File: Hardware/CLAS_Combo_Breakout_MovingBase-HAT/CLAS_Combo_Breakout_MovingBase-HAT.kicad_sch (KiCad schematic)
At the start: 61 parts, among them J1 USB_C_Receptacle_USB2.0, J2 ZED, J3 NEO, U1 USBLC6-2P6

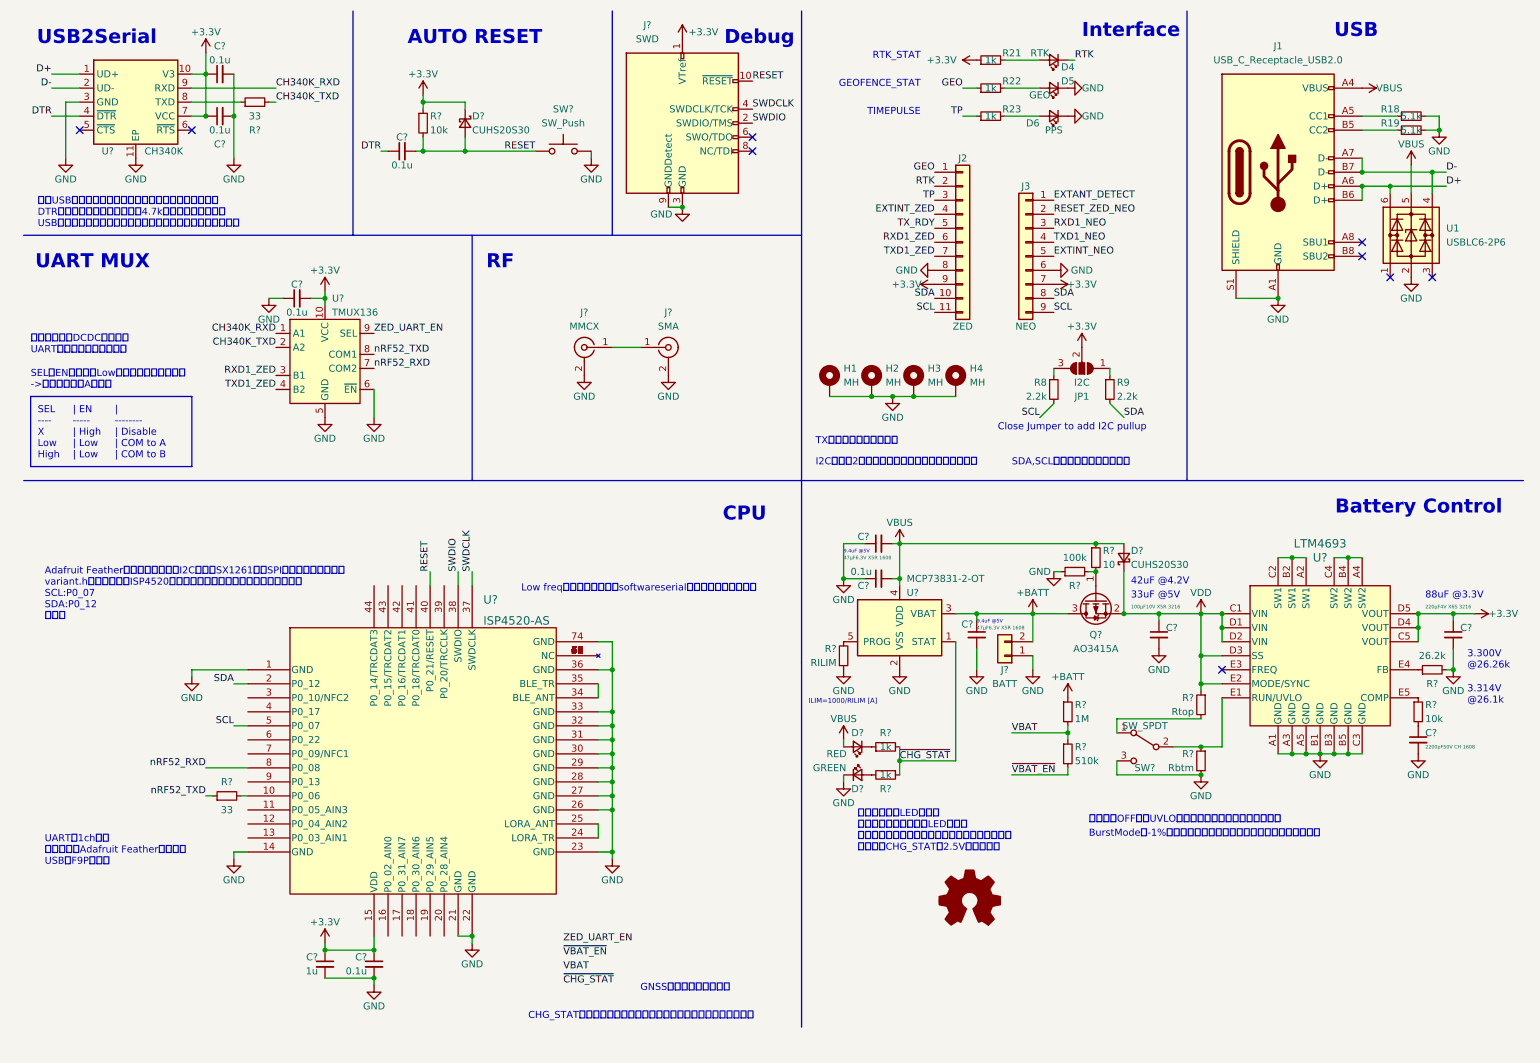
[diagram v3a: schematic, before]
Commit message: アノテーション完了、一部のピンは仮結線
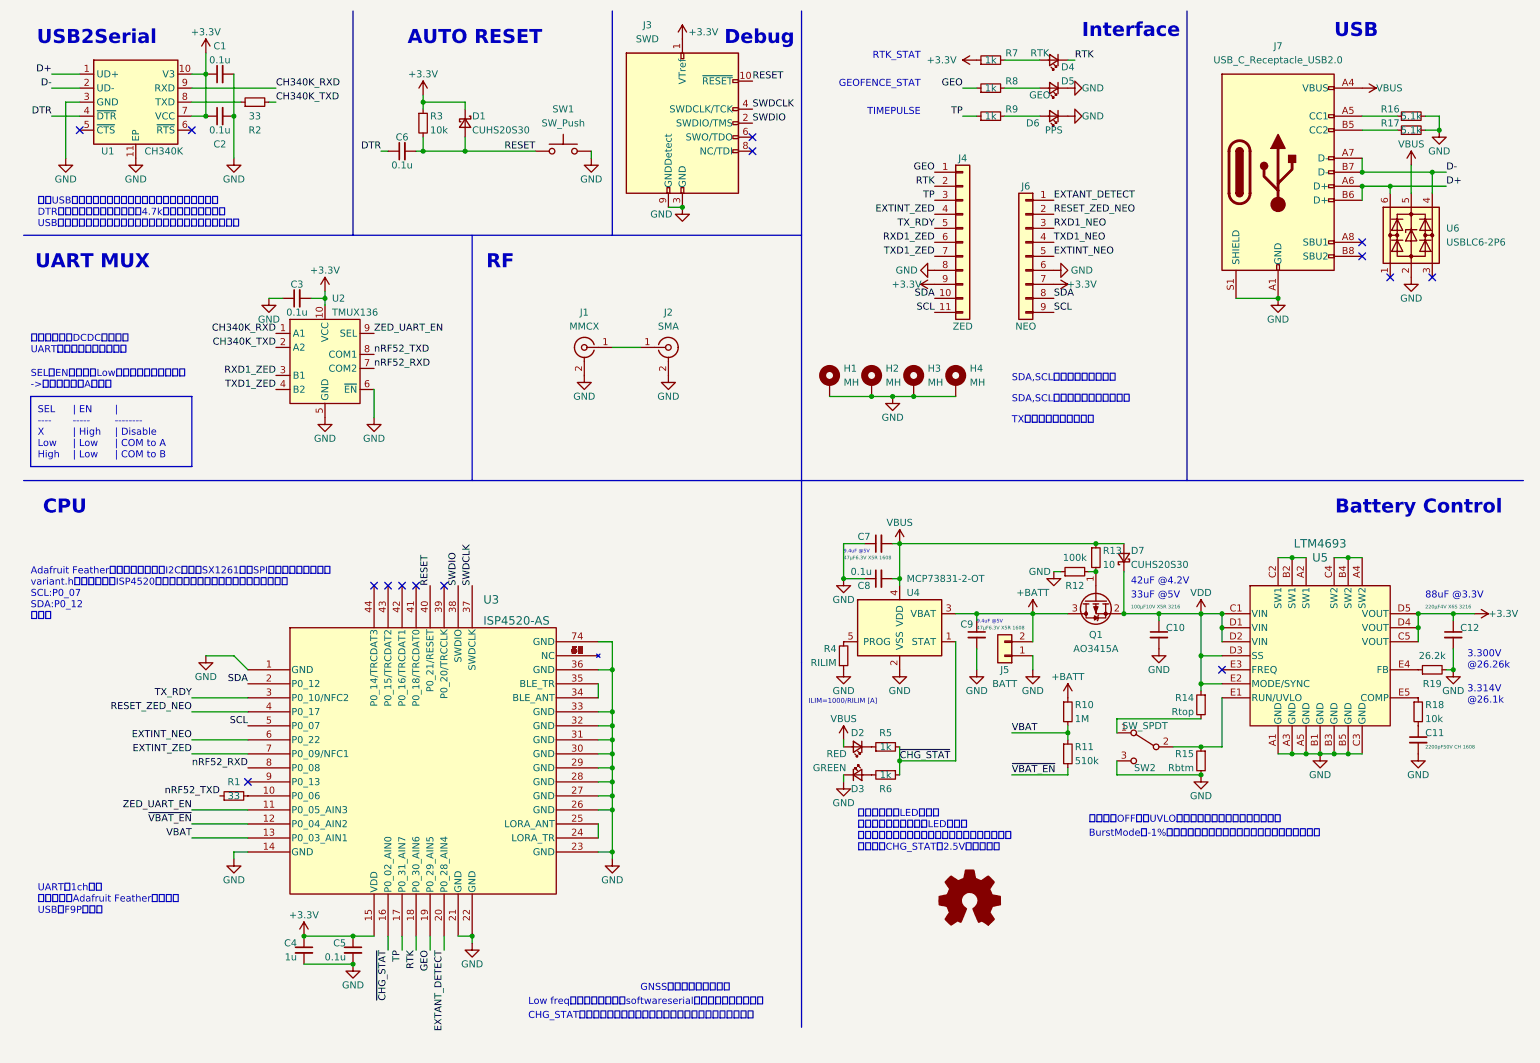
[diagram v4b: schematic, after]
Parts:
- removed JP1: I2C, Jumper_extlib:SolderJumper-3_Open_RoundedPad, symbol Jumper:SolderJumper_3_Open
- removed R8, R9: 2.2k, Resistor_SMD:R_0603_1608Metric, symbol Device:R_Small
- gave numbers to parts that had none: 42
- renumbered J2 to J4, J3 to J6, J1 to J7, R18 to R16, R19 to R17, R21 to R7, R22 to R8, R23 to R9, U1 to U6
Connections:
- net EXTANT_DETECT: now also U3.20 (P0_28_AIN4)
- net EXTINT_NEO: now also U3.6 (P0_22)
- net EXTINT_ZED: now also U3.7 (P0_09/NFC1)
- net GEO: now also U3.19 (P0_29_AIN5)
- net RESET_ZED_NEO: now also U3.4 (P0_17)
- net RTK: now also U3.18 (P0_30_AIN6)
- net TP: now also U3.17 (P0_31_AIN7)
- net TX_RDY: now also U3.3 (P0_10/NFC2)
- net VBAT: now also U3.13 (P0_03_AIN1)
- net ZED_UART_EN: now also U3.11 (P0_05_AIN3)
- net ~{CHG_STAT}: now also U3.16 (P0_02_AIN0)
- net ~{VBAT_EN}: now also U3.12 (P0_04_AIN2)
- no-connect marks 9 -> 15
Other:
- note added: "SDA,SCLは片方だけ配線する"
- note removed: "Close Jumper to add I2C pullup"
- note removed: "I2Cピンは2セットあるから配線しやすい方を使う"
- moved on the sheet: C4, C5, R1

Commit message: フットプリントの割り当て完了
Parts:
- C1, C2, C3, C4, C5, C6, C7, C8, C9: footprint (none) -> Capacitor_SMD:C_0603_1608Metric
- J1: footprint (none) -> Connector_Coaxial_extlib:MMCX_Samtec_MMCX-P-P-H-ST-SM1_Male
- J2: footprint (none) -> Connector_Coaxial_extlib:SMA_Molex_0732512440_embed
- J3: footprint (none) -> Connector_PinHeader_1.27mm:PinHeader_2x05_P1.27mm_Horizontal
- J5: footprint (none) -> Connector_JST:JST_PH_S2B-PH-K_1x02_P2.00mm_Horizontal
- Q1: footprint (none) -> Package_TO_SOT_SMD:SOT-23
- R1, R10, R11, R13, R14, R15, R18, R2, R3, R4: footprint (none) -> Resistor_SMD:R_0603_1608Metric
- SW1: footprint (none) -> Button_Switch_SMD:SW_Push_1P1T_NO_Vertical_Wuerth_434133025816
- SW2: footprint (none) -> Button_Switch_THT_extlib:NKK_SS-12SDP2
- U1: footprint (none) -> Package_SO:SSOP-10_3.9x4.9mm_P1.00mm
- U2: footprint (none) -> Package_DFN_QFN:Texas_R-PUQFN-N10
- U3: footprint (none) -> RF_Module_extlib:ISP4520-AS
- U5: footprint (none) -> Converter_DCDC_extlib:Converter_DCDC_AnalogDevices_LTM4693

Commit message: 配線４割
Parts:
- J3: footprint Connector_PinHeader_1.27mm:PinHeader_2x05_P1.27mm_Horizontal -> Connector_PinHeader_1.27mm:PinHeader_2x05_P1.27mm_Vertical
- J5: footprint Connector_JST:JST_PH_S2B-PH-K_1x02_P2.00mm_Horizontal -> Connector_JST:JST_PH_S2B-PH-SM4-TB_1x02-1MP_P2.00mm_Horizontal
- SW2: footprint Button_Switch_THT_extlib:NKK_SS-12SDP2 -> Button_Switch_SMD_extlib:SW_SPDT_SSSS213202
- U3: footprint RF_Module_extlib:ISP4520-AS -> RF_Module_extlib:ISP4520-AS_with_Keep-Out
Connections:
- net D+: now also U6.1 (I/O1)
- net D-: now also U6.3 (I/O2)
- net EXTANT_DETECT: now also U3.4 (P0_17); no longer U3.20 (P0_28_AIN4)
- net EXTINT_ZED: now also U3.18 (P0_30_AIN6); no longer U3.7 (P0_09/NFC1)
- net GEO: now also U3.13 (P0_03_AIN1); no longer U3.19 (P0_29_AIN5)
- net RESET_ZED_NEO: now also U3.3 (P0_10/NFC2); no longer U3.4 (P0_17)
- net RTK: now also U3.16 (P0_02_AIN0); no longer U3.18 (P0_30_AIN6)
- net SCL: no longer J6.9 (Pin_9)
- net SDA: no longer J6.8 (Pin_8)
- net TX_RDY: now also U3.20 (P0_28_AIN4); no longer U3.3 (P0_10/NFC2)
- net VBAT: now also U3.12 (P0_04_AIN2); no longer U3.13 (P0_03_AIN1)
- net ZED_UART_EN: now also U3.7 (P0_09/NFC1); no longer U3.11 (P0_05_AIN3)
- net ~{CHG_STAT}: now also U3.19 (P0_29_AIN5); no longer U3.16 (P0_02_AIN0)
- net ~{VBAT_EN}: now also U3.11 (P0_05_AIN3); no longer U3.12 (P0_04_AIN2)

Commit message: ちょっと配線した
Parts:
- removed C3: 0.1u, Capacitor_SMD:C_0603_1608Metric, symbol Device:C_Small
- removed H4: MH, MountingHole:MountingHole_2.2mm_M2_Pad_Via, symbol Mechanical:MountingHole_Pad
- removed J6: NEO, Connector_PinHeader_2.54mm:PinHeader_1x09_P2.54mm_Vertical, symbol Connector_Generic:Conn_01x09
- added J6: NEO, Connector_PinHeader_2.54mm:PinHeader_1x07_P2.54mm_Vertical, symbol Connector_Generic:Conn_01x07
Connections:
- net +3.3V: now also J6.7 (Pin_7)
- net EXTANT_DETECT: now also J6.1 (Pin_1)
- net EXTINT_NEO: now also J6.5 (Pin_5)
- net GEO: now also U3.11 (P0_05_AIN3); no longer U3.13 (P0_03_AIN1)
- net GND: now also J6.6 (Pin_6)
- net RESET_ZED_NEO: now also J6.2 (Pin_2)
- net RXD1_NEO: now also J6.3 (Pin_3)
- net TXD1_NEO: now also J6.4 (Pin_4)
- net VBAT: now also U3.13 (P0_03_AIN1); no longer U3.12 (P0_04_AIN2)
- net ~{VBAT_EN}: now also U3.12 (P0_04_AIN2); no longer U3.11 (P0_05_AIN3)
- no-connect marks 15 -> 13
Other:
- note added: "パスコンは実装面積の都合でC1を共有"

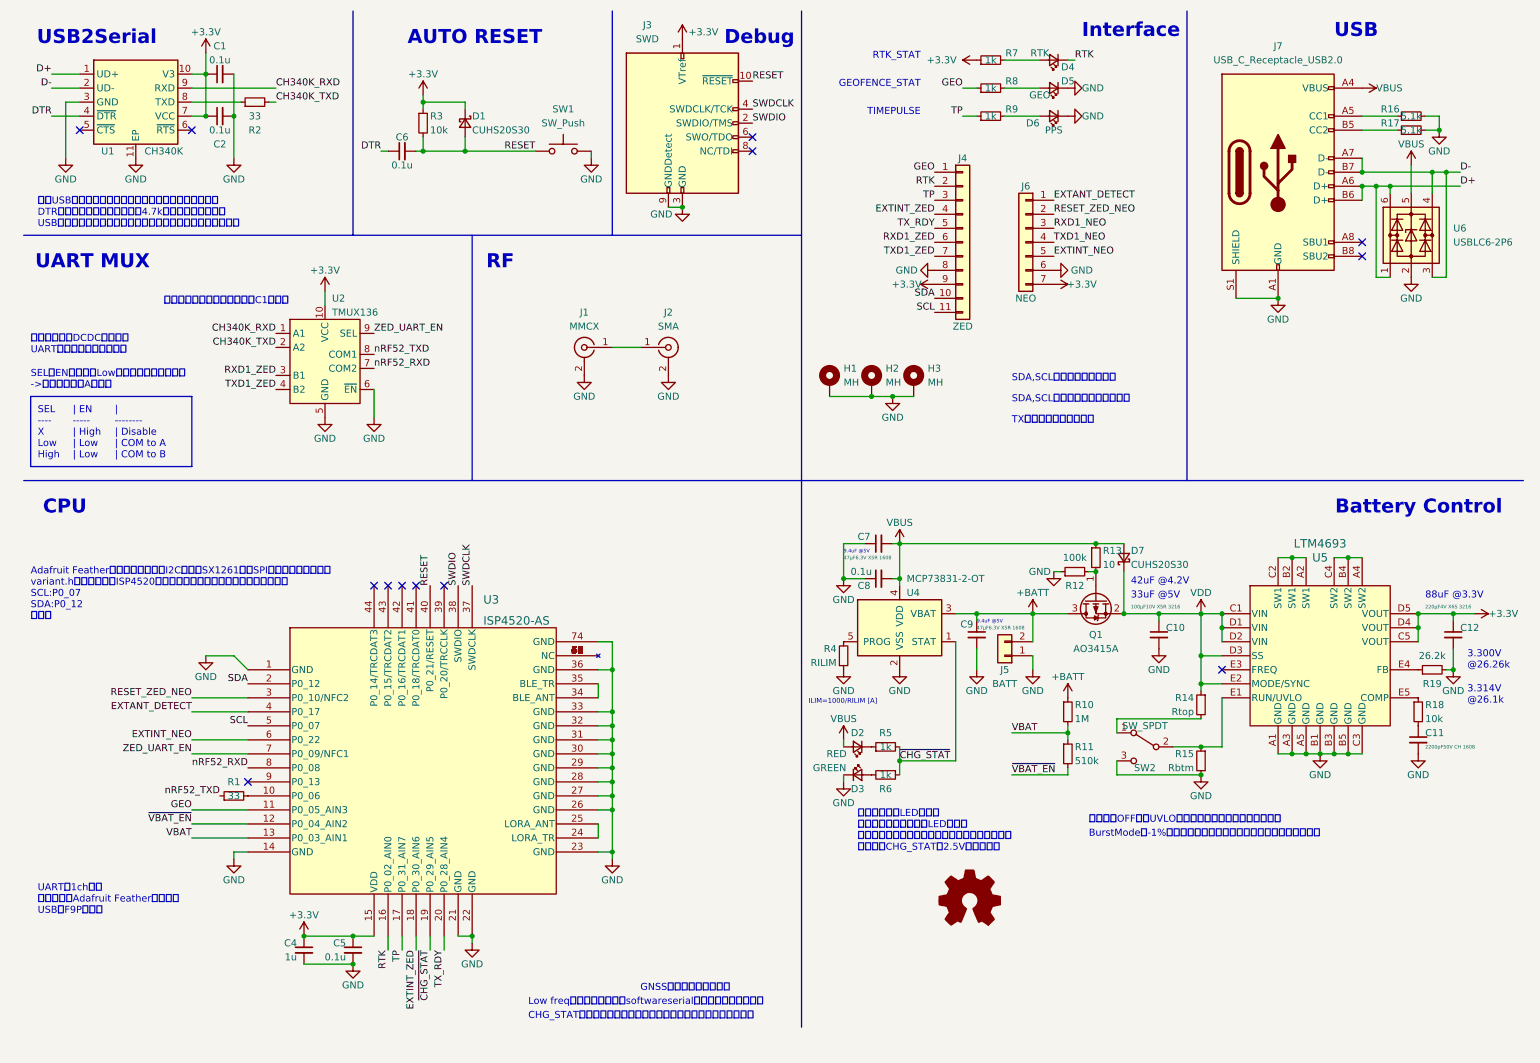
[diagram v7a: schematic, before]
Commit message: MUXをSP3Tのものに変更しRS485経由での補正データの送受信に対応する回路図を書いた
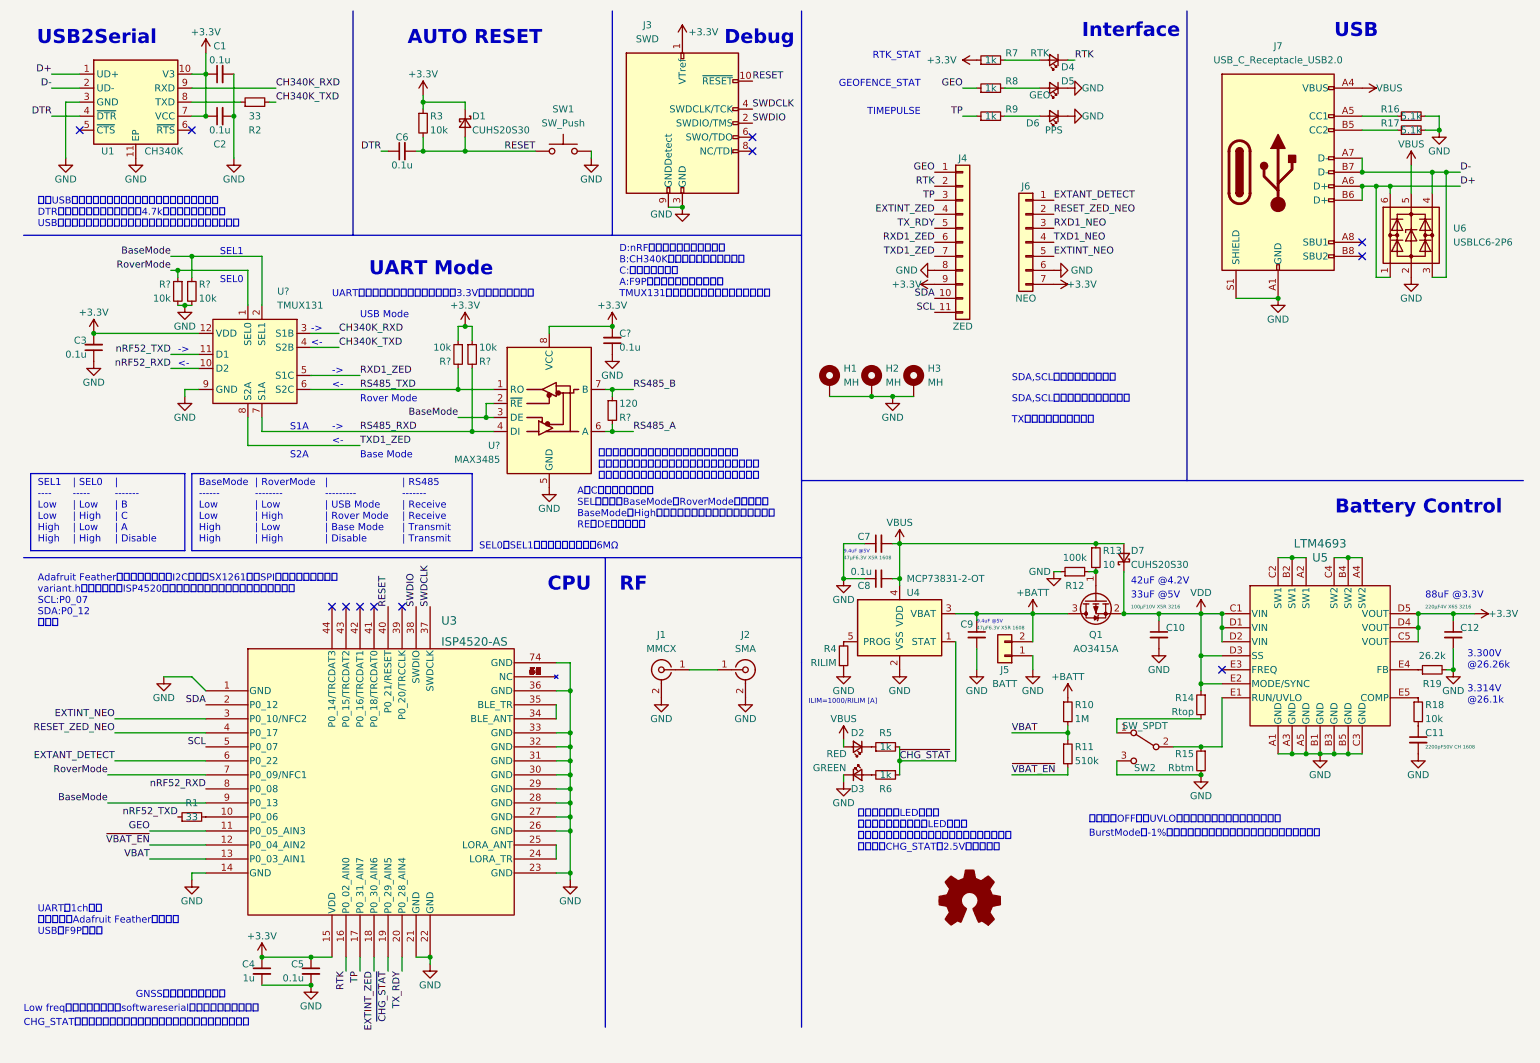
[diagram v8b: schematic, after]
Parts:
- removed U2: TMUX136, Package_DFN_QFN:Texas_R-PUQFN-N10, symbol Analog_Switch_extlib:TMUX136
- added C3, C?: 0.1u, Capacitor_SMD:C_0603_1608Metric, symbol Device:C_Small
- added R? (x4): 10k, Resistor_SMD:R_0603_1608Metric, symbol Device:R_Small
- added R?: 120, Resistor_SMD:R_0603_1608Metric, symbol Device:R_Small
- added U?: TMUX131, symbol Analog_Switch_extlib:TMUX131
- added U?: MAX3485, symbol Interface_UART:MAX3485
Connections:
- net +3.3V: now also C3.2, C?.2, R?.1, R?.1, U?.12 (VDD), U?.8 (VCC)
- net CH340K_RXD: now also U?.3 (S1B)
- net CH340K_TXD: now also U?.4 (S2B)
- net EXTANT_DETECT: now also U3.6 (P0_22); no longer U3.4 (P0_17)
- net EXTINT_NEO: now also U3.3 (P0_10/NFC2); no longer U3.6 (P0_22)
- net GND: now also C3.1, C?.1, R?.2, R?.2, U?.5 (GND), U?.9 (GND)
- net RESET_ZED_NEO: now also U3.4 (P0_17); no longer U3.3 (P0_10/NFC2)
- net RXD1_ZED: now also U?.5 (S1C)
- net TXD1_ZED: now also U?.8 (S2A)
- net nRF52_RXD: now also U?.10 (D2)
- net nRF52_TXD: now also U?.11 (D1)
- net BaseMode: now reaches U3.9 (P0_13)
- net BaseMode: now also R?.1, U?.2 (SEL1), U?.2 (~{RE}), U?.3 (DE)
- net ZED_UART_EN renamed RoverMode
- net RoverMode: now also R?.1, U?.1 (SEL0)
- new net RS485_A: R?.2, U?.6 (A)
- new net RS485_B: R?.1, U?.7 (B)
- new net RS485_RXD: R?.2, U?.4 (DI), U?.7 (S1A)
- new net RS485_TXD: R?.2, U?.1 (RO), U?.6 (S2C)
- no-connect marks 13 -> 12
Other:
- note added: "->"
- note added: "<-"
- note added: "AとCを逆にする場合は SELに繋がるBaseModeとRoverModeを逆にする BaseModeがHighのときに送信するのは変わらないので REとDEはそのまま"
- note added: "Base Mode"
- note added: "BaseMode ------ Low Low High High"
- note added: "D:nRF側送信端だけダンピング B:CH340K側送信端だけダンピング C:ダンピングなし A:F9P送信端にダンピングあり TMUX131側送信端のダンピングは全て省略"
- note added: "Rover Mode"
- note added: "S1A"
- note added: "S2A"
- note added: "SEL0"
- note added: "SEL0とSEL1の内部プルダウンは6MΩ"
- note added: "SEL1"
- note added: "SEL1 ---- Low Low High High"
- note added: "UART Mode"
- note added: "UARTは正論理だが信号が無いときは3.3Vなのでプルアップ"
- note added: "USB Mode"
- note added: "| ------- | B | C | A | Disable"
- note added: "| --------- | USB Mode | Rover Mode | Base Mode | Disable"
- note added: "| RS485 ------- | Receive | Receive | Transmit | Transmit"
- note added: "| RoverMode -------- | Low | High | Low | High"
- note added: "| SEL0 ----- | Low | High | Low | High"
- note added: "差動にプルアップ／ダウン抵抗を付ける場合 片側のみになるためハード的に対称では無くなる上 ドライバの負荷が増えたり通信が遅くなったりする"
- note removed: "SEL ---- X Low High"
- note removed: "SELとENは内部でLowにプルダウンされてる ->デフォルトでAが有効"
- note removed: "UART MUX"
- note removed: "| -------- | Disable | COM to A | COM to B"
- note removed: "| EN ----- | High | Low | Low"
- note removed: "スイッチングDCDCの近くに UARTを通さないようにする"
- note removed: "パスコンは実装面積の都合でC1を共有"
- moved on the sheet: C4, C5, J1, J2, R1, U3
